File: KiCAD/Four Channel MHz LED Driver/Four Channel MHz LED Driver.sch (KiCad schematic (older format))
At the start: 90 parts, among them J1 Barrel_Jack_Switch, J10 Conn_01x08_Female, J2 Conn_01x02_Female, J3 8P8C_Shielded_x4, J4 Conn_01x05_Female, J5 Conn_01x24_Female, J6 Conn_01x03_Male, J7 Conn_01x24_Female, J8 Conn_01x03_Female, J9 Conn_01x03_Female, M1 Fan_4pin, Q2 SUM70060E, SW1 SW_SPDT, SW2 Pushbutton_with_LED_-_ELUMOAT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, SW3 Pushbutton_with_LED_-_ELUMOAT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, SW4 Pushbutton_with_LED_-_ELUMOAT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, SW5 Pushbutton_with_LED_-_ELUMOAT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, U1 12V boost, U10 LT6200CS8-10, U14 Teensy3.6, U16 SN74LV4T125PWR, U2 ASSR-1218, U3 DPBW06F-05, U4 BDJ0GA5WEFJ-E2, U5 ADP7182AUJZ-1.8-R7, U6 TMUX1204DGSR, U7 ASSR-1218, U8 ASSR-1218, U9 ASSR-1218

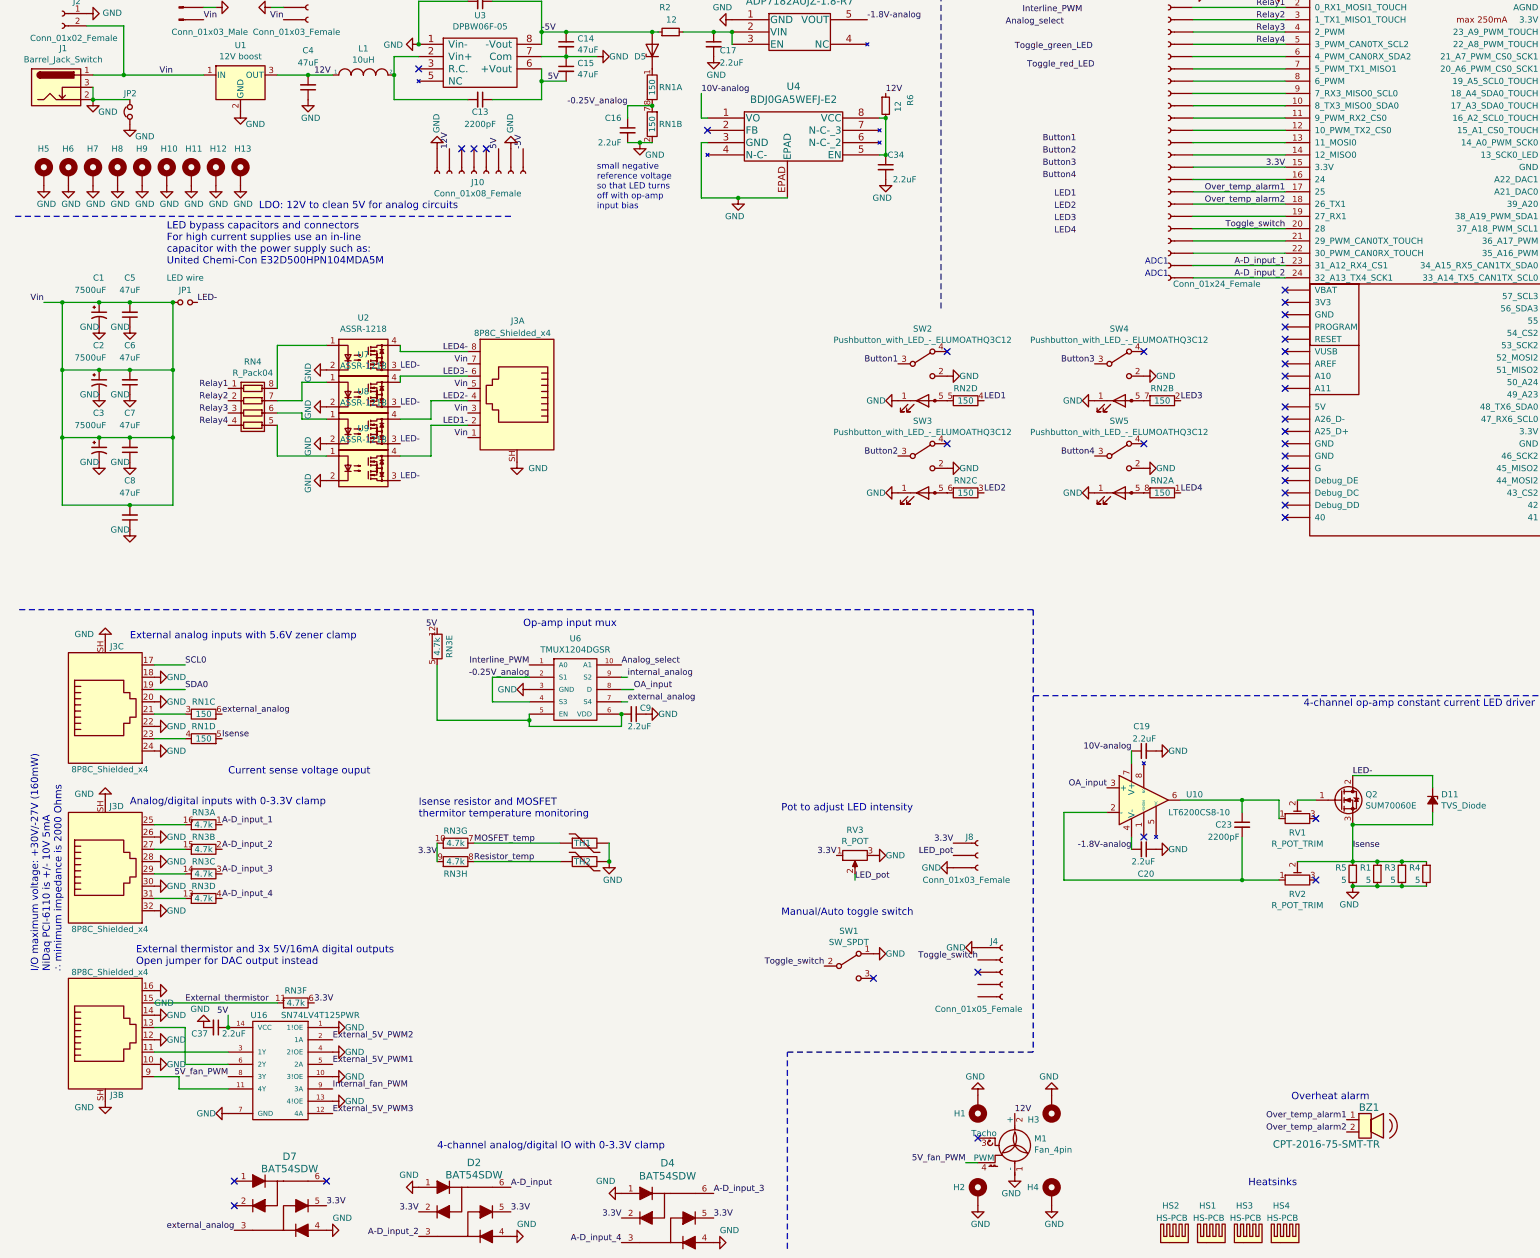
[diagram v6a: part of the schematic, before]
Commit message: stacked standoffs and high current jumpers added
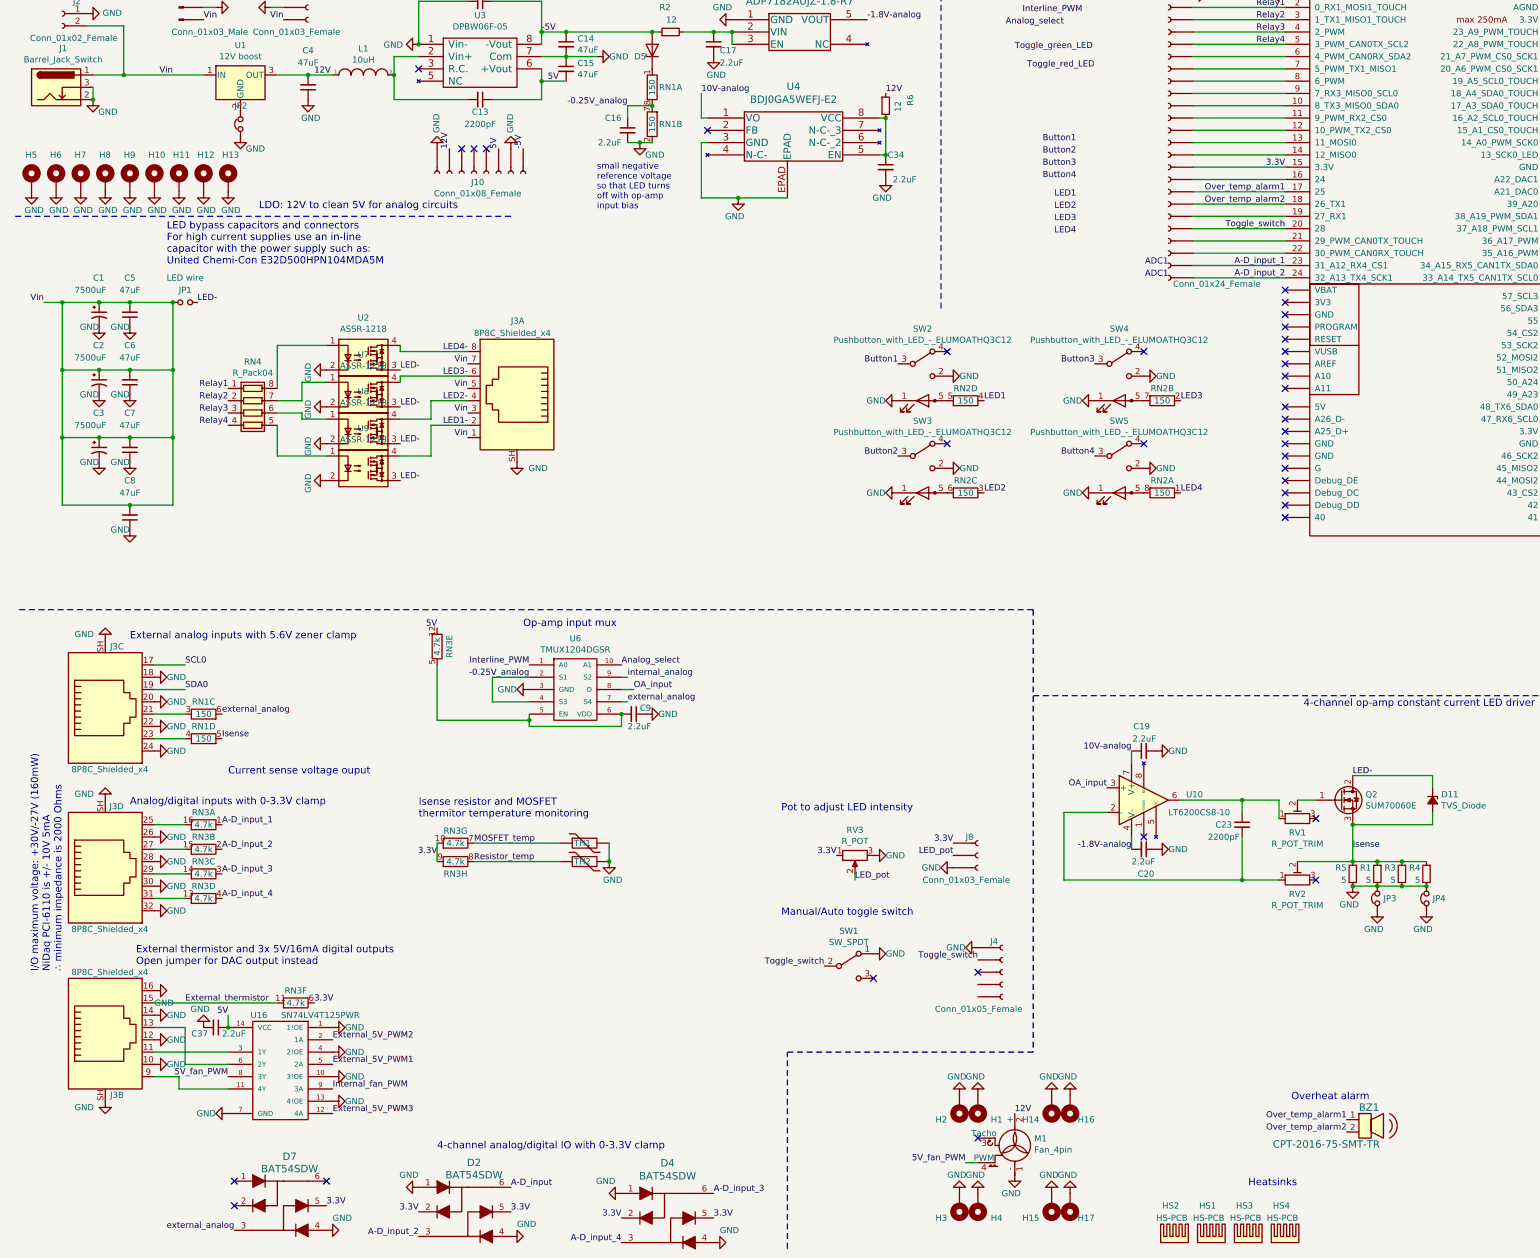
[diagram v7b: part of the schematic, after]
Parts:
- added H14, H15, H16, H17: MountingHole_Pad, Custom Footprints:Ref_only, symbol Mechanical:MountingHole_Pad
- added JP3, JP4: Jumper_NC_Small, Custom Footprints:20A_shunt_5104, symbol Device:Jumper_NC_Small
- H1, H2, H3, H4: Manufacturer Würth Elektronik -> Keystone Electronics; Part # 971300476 -> 24354
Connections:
- net GND: now also H14.1, H15.1, H16.1, H17.1, JP3.1, JP3.2, JP4.1, JP4.2; no longer JP2.2, U1.2 (GND)
- new net: JP2.2, U1.2 (GND)
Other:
- moved on the sheet: H10, H11, H12, H13, H5, H6, H7, H8, H9, JP2

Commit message: Routing User inputs
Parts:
- removed H10, H11, H12, H13, H5, H6, H7, H8, H9: MountingHole_Pad, Custom Footprints:Ground_Via, symbol Mechanical:MountingHole_Pad
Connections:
- net A-D_input_1: no longer J5.~, U14.23 (31_A12_RX4_CS1)
- net A-D_input_2: no longer J5.~, U14.24 (32_A13_TX4_SCK1)
- net A-D_input_3: no longer J7.~, U14.30 (33_A14_TX5_CAN1TX_SCL0)
- net A-D_input_4: no longer J7.~, U14.31 (34_A15_RX5_CAN1TX_SDA0)
- net Button1: now also J5.~, U14.17 (25)
- net Button2: now also J5.~, U14.19 (27_RX1)
- net Button3: now also J5.~, U14.21 (29_PWM_CAN0TX_TOUCH)
- net External_thermistor: no longer J7.~, U14.38 (A22_DAC1)
- net GND: now also JP2.2, U1.2 (GND)
- net Internal_Isense: no longer J7.~, U14.41 (14_A0_PWM_SCK0)
- net LED1: now also J5.~, U14.18 (26_TX1)
- net LED2: now also J5.~, U14.20 (28)
- net LED3: now also J5.~, U14.22 (30_PWM_CAN0RX_TOUCH)
- net LED4: now also J5.~, U14.23 (31_A12_RX4_CS1)
- net LED_pot: now also U14.30 (33_A14_TX5_CAN1TX_SCL0); no longer U14.44 (17_A3_SDA0_TOUCH)
- net Over_temp_alarm1: now also U14.24 (32_A13_TX4_SCK1); no longer U14.17 (25)
- net Over_temp_alarm2: no longer J5.~, U14.18 (26_TX1)
- net Resistor_temp: no longer J7.~, U14.33 (36_A17_PWM)
- net Toggle_switch: now also U14.16 (24); no longer U14.20 (28)
- net Pushbutton_LED: no longer names the net of J7.~, U14.35 (38_A19_PWM_SDA1)
- net Resistor_temp_2: no longer names the net of J7.~, U14.34 (37_A18_PWM_SCL1)
- new net: J7.~, U14.31 (34_A15_RX5_CAN1TX_SDA0)
- new net: J7.~, U14.33 (36_A17_PWM)
- new net: J7.~, U14.38 (A22_DAC1)
- new net: J7.~, U14.41 (14_A0_PWM_SCK0)
- new net: J7.~, U14.44 (17_A3_SDA0_TOUCH)
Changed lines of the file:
@@
 Wire Notes Line
 	8750 6700 16050 6700
-Text Label 8700 1600 0    50   ~ 0
-Toggle_red_LED
-Text Label 8600 1450 0    50   ~ 0
-Toggle_green_LED
-Text Label 10800 2600 2    50   ~ 0
+Text Label 10800 3300 2    50   ~ 0
 Over_temp_alarm1
-Text Label 10800 3200 2    50   ~ 0
+Text Label 8650 3100 2    50   ~ 0
 A-D_input_1
-Text Label 10800 3300 2    50   ~ 0
+Text Label 8650 3200 2    50   ~ 0
 A-D_input_2
-Text Label 13100 3300 0    50   ~ 0
+Text Label 8650 3300 2    50   ~ 0
 A-D_input_3
-Text Label 13100 3200 0    50   ~ 0
+Text Label 8650 3400 2    50   ~ 0
 A-D_input_4
 Text Label 2150 7750 0    50   ~ 0
@@
 Text Label 5400 11150 2    50   ~ 0
 A-D_input_4
-Text Label 13100 1900 0    50   ~ 0
+Text Label 13100 3300 0    50   ~ 0
 LED_pot
-Text Label 15050 2750 0    50   ~ 0
+Text Label 8600 2850 2    50   ~ 0
 MOSFET_temp
-Text Label 13100 3000 0    50   ~ 0
+Text Label 8600 2750 2    50   ~ 0
 Resistor_temp
 $Comp
@@
 	-1   0    0    -1
 $EndComp
-Text Label 10800 2900 2    50   ~ 0
+Text Label 10800 2500 2    50   ~ 0
 Toggle_switch
-Text Label 13100 2200 0    50   ~ 0
+Text Label 8950 1700 2    50   ~ 0
 Internal_Isense
 Wire Wire Line
@@
 	1    0    0    -1
 $EndComp
-Text Label 10800 2700 2    50   ~ 0
+Text Label 9050 800  2    50   ~ 0
 Over_temp_alarm2
 Text Label 11300 10150 2    50   ~ 0
@@
 	1    0    0    -1
 $EndComp
-Text Label 13100 2500 0    50   ~ 0
+Text Label 8950 2000 2    50   ~ 0
 External_thermistor
 Wire Wire Line
@@
 	0    -1   1    0
 $EndComp
-Text Label 13100 2800 0    50   ~ 0
-Pushbutton_LED
 Connection ~ 11350 8050
 Wire Wire Line
@@
 Wire Notes Line
 	500  6000 8750 6000
-Text Label 13100 2900 0    50   ~ 0
-Resistor_temp_2
 Text Label 4150 4000 2    50   ~ 0
 Vin
@@
 	0    1    1    0
 $EndComp
-Text Label 9100 2200 2    50   ~ 0
+Text Label 10800 2600 2    50   ~ 0
 Button1
-Text Label 9100 2300 2    50   ~ 0
+Text Label 10800 2800 2    50   ~ 0
 Button2
-Text Label 9100 2400 2    50   ~ 0
+Text Label 10800 3000 2    50   ~ 0
 Button3
-Text Label 9100 2500 2    50   ~ 0
+Text Label 9500 1700 2    50   ~ 0
 Button4
 Text Label 7650 4000 2    50   ~ 0
@@
 Text Label 9250 4750 2    50   ~ 0
 Button4
-Text Label 9100 2650 2    50   ~ 0
+Text Label 10800 2700 2    50   ~ 0
 LED1
-Text Label 9100 2750 2    50   ~ 0
+Text Label 10800 2900 2    50   ~ 0
 LED2
-Text Label 9100 2850 2    50   ~ 0
+Text Label 10800 3100 2    50   ~ 0
 LED3
-Text Label 9100 2950 2    50   ~ 0
+Text Label 10800 3200 2    50   ~ 0
 LED4
 Text Label 8350 4300 0    50   ~ 0
@@
 U 1 1 5F56E8CF
 P 2300 2050
-F 0 "JP2" V 2450 2100 50  0000 R CNN
+F 0 "JP2" V 2300 2050 50  0000 R CNN
 F 1 "Jumper_NC_Small" V 2255 2003 50  0001 R CNN
 F 2 "Resistor_SMD:R_1206_3216Metric" H 2300 2050 50  0001 C CNN
@@
 	1    2300 2050
 	0    -1   -1   0
-$EndComp
-$Comp
-L power:GND #PWR0165
-U 1 1 5F581B5A
-P 600 2600
-F 0 "#PWR0165" H 600 2350 50  0001 C CNN
-F 1 "GND" H 700 2450 50  0000 R CNN
-F 2 "" H 600 2600 50  0001 C CNN
-F 3 "" H 600 2600 50  0001 C CNN
-	1    600  2600
-	1    0    0    -1
 $EndComp
 Wire Wire Line
@@
 External_5V_PWM1
 $Comp
-L Mechanical:MountingHole_Pad H5
-U 1 1 5FA26710
-P 600 2500
-F 0 "H5" H 550 2700 50  0000 L CNN
-F 1 "MountingHole_Pad" H 700 2458 50  0001 L CNN
-F 2 "Custom Footprints:Ground_Via" H 600 2500 50  0001 C CNN
-F 3 "~" H 600 2500 50  0001 C CNN
-	1    600  2500
-	1    0    0    -1
-$EndComp
-$Comp
-L power:GND #PWR0114
-U 1 1 5FA5209D
-P 800 2600
-F 0 "#PWR0114" H 800 2350 50  0001 C CNN
-F 1 "GND" H 900 2450 50  0000 R CNN
-F 2 "" H 800 2600 50  0001 C CNN
-F 3 "" H 800 2600 50  0001 C CNN
-	1    800  2600
-	1    0    0    -1
-$EndComp
-$Comp
-L Mechanical:MountingHole_Pad H6
-U 1 1 5FA520A3
-P 800 2500
-F 0 "H6" H 750 2700 50  0000 L CNN
-F 1 "MountingHole_Pad" H 900 2458 50  0001 L CNN
-F 2 "Custom Footprints:Ground_Via" H 800 2500 50  0001 C CNN
-F 3 "~" H 800 2500 50  0001 C CNN
-	1    800  2500
-	1    0    0    -1
-$EndComp
-$Comp
-L power:GND #PWR0157
-U 1 1 5FA5EACA
-P 1000 2600
-F 0 "#PWR0157" H 1000 2350 50  0001 C CNN
-F 1 "GND" H 1100 2450 50  0000 R CNN
-F 2 "" H 1000 2600 50  0001 C CNN
-F 3 "" H 1000 2600 50  0001 C CNN
-	1    1000 2600
-	1    0    0    -1
-$EndComp
-$Comp
-L Mechanical:MountingHole_Pad H7
-U 1 1 5FA5EAD0
-P 1000 2500
-F 0 "H7" H 950 2700 50  0000 L CNN
-F 1 "MountingHole_Pad" H 1100 2458 50  0001 L CNN
-F 2 "Custom Footprints:Ground_Via" H 1000 2500 50  0001 C CNN
-F 3 "~" H 1000 2500 50  0001 C CNN
-	1    1000 2500
-	1    0    0    -1
-$EndComp
-$Comp
-L power:GND #PWR0158
-U 1 1 5FA6B549
-P 1200 2600
-F 0 "#PWR0158" H 1200 2350 50  0001 C CNN
-F 1 "GND" H 1300 2450 50  0000 R CNN
-F 2 "" H 1200 2600 50  0001 C CNN
-F 3 "" H 1200 2600 50  0001 C CNN
-	1    1200 2600
-	1    0    0    -1
-$EndComp
-$Comp
-L Mechanical:MountingHole_Pad H8
-U 1 1 5FA6B54F
-P 1200 2500
-F 0 "H8" H 1150 2700 50  0000 L CNN
-F 1 "MountingHole_Pad" H 1300 2458 50  0001 L CNN
-F 2 "Custom Footprints:Ground_Via" H 1200 2500 50  0001 C CNN
-F 3 "~" H 1200 2500 50  0001 C CNN
-	1    1200 2500
-	1    0    0    -1
-$EndComp
-$Comp
-L power:GND #PWR0166
-U 1 1 5FA77F30
-P 1400 2600
-F 0 "#PWR0166" H 1400 2350 50  0001 C CNN
-F 1 "GND" H 1500 2450 50  0000 R CNN
-F 2 "" H 1400 2600 50  0001 C CNN
-F 3 "" H 1400 2600 50  0001 C CNN
-	1    1400 2600
-	1    0    0    -1
-$EndComp
-$Comp
-L Mechanical:MountingHole_Pad H9
-U 1 1 5FA77F36
-P 1400 2500
-F 0 "H9" H 1350 2700 50  0000 L CNN
-F 1 "MountingHole_Pad" H 1500 2458 50  0001 L CNN
-F 2 "Custom Footprints:Ground_Via" H 1400 2500 50  0001 C CNN
-F 3 "~" H 1400 2500 50  0001 C CNN
-	1    1400 2500
-	1    0    0    -1
-$EndComp
-$Comp
-L power:GND #PWR0167
-U 1 1 5FA84A05
-P 1600 2600
-F 0 "#PWR0167" H 1600 2350 50  0001 C CNN
-F 1 "GND" H 1700 2450 50  0000 R CNN
-F 2 "" H 1600 2600 50  0001 C CNN
-F 3 "" H 1600 2600 50  0001 C CNN
-	1    1600 2600
-	1    0    0    -1
-$EndComp
-$Comp
-L Mechanical:MountingHole_Pad H10
-U 1 1 5FA84A0B
-P 1600 2500
-F 0 "H10" H 1550 2700 50  0000 L CNN
-F 1 "MountingHole_Pad" H 1700 2458 50  0001 L CNN
-F 2 "Custom Footprints:Ground_Via" H 1600 2500 50  0001 C CNN
-F 3 "~" H 1600 2500 50  0001 C CNN
-	1    1600 2500
-	1    0    0    -1
-$EndComp
-$Comp
-L power:GND #PWR0168
-U 1 1 5FA91550
-P 1800 2600
-F 0 "#PWR0168" H 1800 2350 50  0001 C CNN
-F 1 "GND" H 1900 2450 50  0000 R CNN
-F 2 "" H 1800 2600 50  0001 C CNN
-F 3 "" H 1800 2600 50  0001 C CNN
-	1    1800 2600
-	1    0    0    -1
-$EndComp
-$Comp
-L Mechanical:MountingHole_Pad H11
-U 1 1 5FA91556
-P 1800 2500
-F 0 "H11" H 1750 2700 50  0000 L CNN
-F 1 "MountingHole_Pad" H 1900 2458 50  0001 L CNN
-F 2 "Custom Footprints:Ground_Via" H 1800 2500 50  0001 C CNN
-F 3 "~" H 1800 2500 50  0001 C CNN
-	1    1800 2500
-	1    0    0    -1
-$EndComp
-$Comp
-L power:GND #PWR0170
-U 1 1 5FA9DF11
-P 2000 2600
-F 0 "#PWR0170" H 2000 2350 50  0001 C CNN
-F 1 "GND" H 2100 2450 50  0000 R CNN
-F 2 "" H 2000 2600 50  0001 C CNN
-F 3 "" H 2000 2600 50  0001 C CNN
-	1    2000 2600
-	1    0    0    -1
-$EndComp
-$Comp
-L Mechanical:MountingHole_Pad H12
-U 1 1 5FA9DF17
-P 2000 2500
-F 0 "H12" H 1950 2700 50  0000 L CNN
-F 1 "MountingHole_Pad" H 2100 2458 50  0001 L CNN
-F 2 "Custom Footprints:Ground_Via" H 2000 2500 50  0001 C CNN
-F 3 "~" H 2000 2500 50  0001 C CNN
-	1    2000 2500
-	1    0    0    -1
-$EndComp
-$Comp
 L power:GND #PWR0171
 U 1 1 5FAAAA28
-P 2200 2600
-F 0 "#PWR0171" H 2200 2350 50  0001 C CNN
-F 1 "GND" H 2300 2450 50  0000 R CNN
-F 2 "" H 2200 2600 50  0001 C CNN
-F 3 "" H 2200 2600 50  0001 C CNN
-	1    2200 2600
-	1    0    0    -1
-$EndComp
-$Comp
-L Mechanical:MountingHole_Pad H13
-U 1 1 5FAAAA2E
-P 2200 2500
-F 0 "H13" H 2150 2700 50  0000 L CNN
-F 1 "MountingHole_Pad" H 2300 2458 50  0001 L CNN
-F 2 "Custom Footprints:Ground_Via" H 2200 2500 50  0001 C CNN
-F 3 "~" H 2200 2500 50  0001 C CNN
-	1    2200 2500
-	1    0    0    -1
+P 2300 1950
+F 0 "#PWR0171" H 2300 1700 50  0001 C CNN
+F 1 "GND" H 2400 1800 50  0000 R CNN
+F 2 "" H 2300 1950 50  0001 C CNN
+F 3 "" H 2300 1950 50  0001 C CNN
+	1    2300 1950
+	0    -1   -1   0
 $EndComp
 $Comp
@@
 	-1   0    0    1
 $EndComp
+Connection ~ 2300 1950
 $EndSCHEMATC
